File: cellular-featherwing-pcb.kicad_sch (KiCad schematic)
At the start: 42 parts, among them J1 SIM8060-6-0-14-00-A, J2 TSM-116-01-L-SV, J3 TSM-112-01-L-SV, J4 U.FL-R-SMT(10), J5 U.FL-R-SMT(10), U1 BG96, U2 TPS63020DSJR, U3 TXB0108DQSR, U4 MAX8868EUK30+

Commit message: schematic complete
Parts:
- added C1, C2, C6, C7, C8: 22uF, Capacitor_SMD:C_0603_1608Metric, symbol Device:C
- added C10, C13, C14, C9: DNP, Capacitor_SMD:C_0402_1005Metric, symbol Device:C
- added C12: 100pF, symbol Device:C
- added C15: 0.1uF, Capacitor_SMD:C_0402_1005Metric, symbol Device:C
- added C20, C21: 100nF, Capacitor_SMD:C_0402_1005Metric, symbol Device:C
- added C22, C3: 33pF, Capacitor_SMD:C_0402_1005Metric, symbol Device:C
- added C24, C25: 10pF, Capacitor_SMD:C_0402_1005Metric, symbol Device:C
- added C26, C28: C_Polarized_US, Capacitor_Tantalum_SMD:CP_EIA-3528-12_Kemet-T, symbol Device:C_Polarized_US
- added C3: 2.2uF, symbol Device:C
- added C30, C31, C33: 4.7uF, Capacitor_SMD:C_0402_1005Metric, symbol Device:C
- added C4: 0.1uF, symbol Device:C
- added FB1, FB2, FB3, FB4: FerriteBead, Resistor_SMD:R_0805_2012Metric, symbol Device:FerriteBead
- added L1: 1 uH, Inductor_SMD:L_Coilcraft_XxL4020, symbol pspice:INDUCTOR
- added L2: 47nH, symbol pspice:INDUCTOR
- added R1: 1.24M, symbol Device:R
- added R10, R16, R17: 10k, symbol Device:R
- added R11, R12, RR13: 1k, symbol Device:R
- added R15: 100k, symbol Device:R
- added R2: 182k, symbol Device:R
- added R6: 0, Capacitor_SMD:C_0402_1005Metric, symbol Device:R
- added R7: 10, Capacitor_SMD:C_0603_1608Metric, symbol Device:R
- added SC1, SC2: SolderJumper_2_Bridged, Jumper:SolderJumper-2_P1.3mm_Bridged_RoundedPad1.0x1.5mm, symbol Jumper:SolderJumper_2_Bridged
- added SO1, SO17, SO18, SO2: SolderJumper_2_Open, Jumper:SolderJumper-2_P1.3mm_Open_RoundedPad1.0x1.5mm, symbol Jumper:SolderJumper_2_Open
- added TP1, TP10, TP11, TP12, TP13, TP14, TP15, TP2, TP3, TP4, TP5, TP6, TP7, TP8, TP9: TestPoint, TestPoint:TestPoint_Pad_D1.0mm, symbol Connector:TestPoint
- added VD1, VD2: D_TVS, symbol Device:D_TVS
- added VD5, VD6: SS2030FL_R1_00001, Diode_SMD:D_SOD-123F, symbol Device:D
- J4, J5: value U.FL-R-SMT(10) -> U.FL-R-SMT; Digikey (none) -> https://www.digikey.com/en/products/detail/hirose-electric-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; MP U.FL-R-SMT_10_ -> (none); MPN (none) -> U.FL-R-SMT(10)
- SC3, SC4, SC6, SC7, SO10, SO11, SO12, SO13, SO14, SO15, SO4, SO5, SO6, SO7, SO8: now left out of the parts list
- U1: Digikey (none) -> https://www.digikey.com/en/products/detail/quectel/BG96MA-1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; MPN (none) -> BG96MA-128-SGN
- U2: value TPS63020DSJR -> TPS63020QDSJTQ1; footprint IC_TPS63020DSJR -> TPS63020DSJR:IC_TPS63020DSJR; Availability Good -> (none); DigiKey-Purchase-URL https://snapeda.com/shop?store=DigiKey&id=296571 -> (none); Digikey (none) -> https://www.digikey.com/en/products/detail/texas-instrument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; MF Texas Instruments -> (none); MP TPS63020DSJR -> (none); MPN (none) -> TPS63020QDSJTQ1; Mouser-Purchase-URL https://snapeda.com/shop?store=Mouser&id=296571 -> (none); Package VSON-14 Texas Instruments -> (none); Price None -> (none); Texas_Instruments-Purchase-URL https://snapeda.com/shop?store=Texas+Instruments&id=296571 -> (none)
- U4: value MAX8868EUK30+ -> MAX8868EUK30+T; Digikey (none) -> https://www.digikey.com/en/products/detail/analog-devices-i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; MPN (none) -> MAX8868EUK30+T
- renumbered R2 to R21, R1 to R22
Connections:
- net 3V3: now also U4.4 (OUT), C31.1
- net 5V: now also VD6.2 (A)
- net CTS: now also SC1.2 (B)
- net CTS_GPS_TXD: now also SC1.1 (A), SO1.2 (B)
- net DBG_RXD: now also TP15.1
- net DBG_TXD: now also TP14.1
- net ENABLE: now also U2.12 (EN)
- net GND: now also J4.2, J4.3, J5.2, J5.3, U2.15 (PGND), U2.2 (GND), C1.2, C10.2, C13.2, C14.2, C15.2, C2.2, C20.2, C21.2, C22.2, C24.2, C25.2, C26.2, C28.2, C3.2, C3.2, C30.2, C31.2, C33.2, C4.2, C6.2, C7.2, C8.2, C9.2, R10.1, R15.2, R2.2, TP13.1, VD1.1 (A1), VD2.1 (A1)
- net GPS_ANT: now also C12.2, C14.1
- net GPS_ANT_VDD: now also C15.1, R7.2
- net GPS_RXD: now also SO2.1 (A)
- net GPS_TXD: now also SO1.1 (A)
- net GSM_ANT: now also C13.1, R6.2
- net GSM_CTS: now also TP4.1
- net GSM_DCD: now also TP6.1
- net GSM_DTR: now also TP5.1
- net GSM_RI: now also R11.2, TP7.1
- net GSM_RTS: now also TP3.1
- net GSM_RXD: now also TP2.1
- net GSM_STATUS: now also TP8.1
- net GSM_TXD: now also R12.2, RR13.2, TP1.1
- net I2C_SDA: now also R16.1
- net RI: now also R11.1
- net RTS: now also SC2.2 (B)
- net RTS_GPS_RXD: now also SC2.1 (A), SO2.2 (B)
- net TXD: now also R10.2, R12.1, RR13.1
- net USB_BOOT: now also TP12.1
- net USB_DN_GSM: now also TP11.1
- net USB_DP_GSM: now also TP10.1
- net USB_VBUS_GSM: now also TP9.1
- net VBAT: now also VD5.2 (A)
- net VBAT_RF: now also C20.1, C21.1, C22.1, C24.1, C25.1, C26.1, C28.1, C3.1, FB3.1, FB4.1
- net VDD: now also SO17.2 (B), SO18.2 (B)
- net VMODEM: now reaches U4.1 (~{SHDN})
- net VMODEM: now also U4.3 (IN), C30.1, FB2.2, FB3.2, FB4.2
- net at U4.5 (BP): now also C33.1
- net at J5.1: now also C10.1, C12.1, L2.1, VD2.2 (A2)
- net at J4.1: now also C9.1, R6.1, VD1.2 (A2)
- net at U2.1 (VINA): now also C4.1
- net at U2.10 (VIN_10): now also U2.11 (VIN_11), U2.13 (PS/SYNC), C1.1, C2.1, C3.1, FB1.2, R15.1
- net at U2.3 (FB): now also R1.2, R2.1
- net at U2.4 (VOUT_4): now also U2.5 (VOUT_5), C6.1, C7.1, C8.1, FB2.1, R1.1
- net at U2.6 (L2_6): now also U2.7 (L2_7), L1.1
- net at U2.8 (L1_8): now also U2.9 (L1_9), L1.2
- new net: L2.2, R7.1
- new net: R16.2, SO17.1 (A)
- new net: R17.2, SO18.1 (A)
- new net I2C_SCl: R17.1
- new net VIN: FB1.1, VD5.1 (K), VD6.1 (K)
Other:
- company: (none) -> Ribbit Network
- title: (none) -> Cellular Featherwing PCB
- moved on the sheet: C11, C16, C17, C18, C28, C29, C32, D1, DD1, J1, J4, R14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

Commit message: All footprints assigned
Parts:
- C11, C12, C16, C17, C18, C29, C3, C32, C4, R14: footprint (none) -> Capacitor_SMD:C_0402_1005Metric
- C34: renamed from C28; footprint (none) -> Capacitor_SMD:C_0402_1005Metric
- J2: MPN (none) -> TSM-116-01-L-SV
- J3: MPN (none) -> TSM-112-01-L-SV
- L2: footprint (none) -> Inductor_SMD:L_0402_1005Metric
- R1, R10, R11, R12, R15, R16, R17, R2, R8: footprint (none) -> Resistor_SMD:R_0402_1005Metric
- R13: renamed from RR13; footprint (none) -> Resistor_SMD:R_0402_1005Metric
- R21, R22, R3: footprint (none) -> Resistor_SMD:R_0402_1005Metric; Digikey (none) -> https://www.digikey.com/en/products/detail/yageo/RC0402JR-0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; MPN (none) -> RC0402JR-070RP
- R6: footprint Capacitor_SMD:C_0402_1005Metric -> Resistor_SMD:R_0402_1005Metric
- SC7: footprint (none) -> Jumper:SolderJumper-2_P1.3mm_Bridged_RoundedPad1.0x1.5mm
- VD1, VD2: footprint (none) -> Diode_SMD:D_0402_1005Metric
- VD4: footprint (none) -> LED_SMD:LED_0603_1608Metric; Digikey (none) -> https://www.digikey.com/en/products/detail/w%C3%BCrth-elekt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; MPN (none) -> 150060BS75000
- renumbered C3 to C23

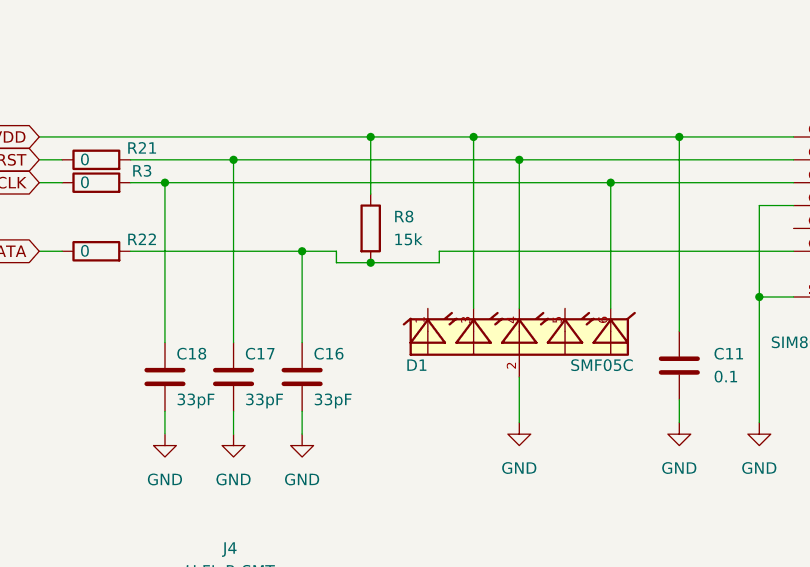
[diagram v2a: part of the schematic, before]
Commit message: Fixed drc and imported to pcb
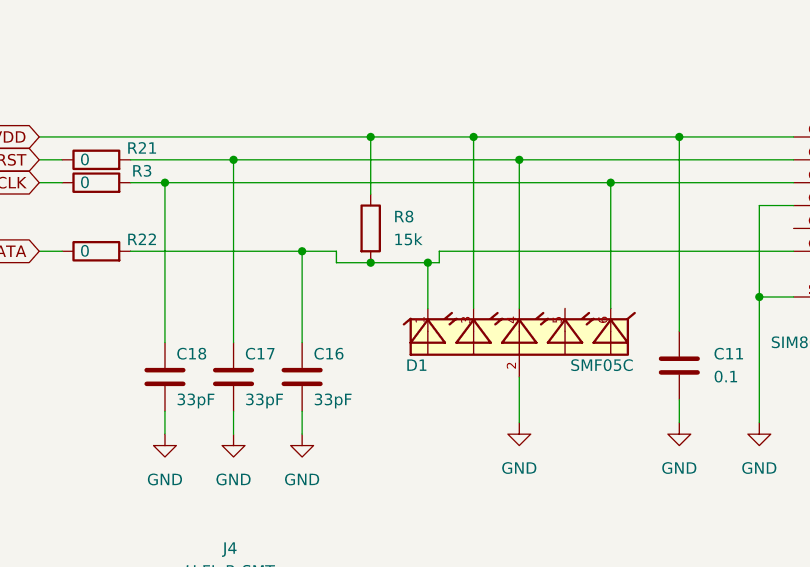
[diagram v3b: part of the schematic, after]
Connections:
- net at C16.1, J1.C7 (IO), R22.2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: now also D1.1
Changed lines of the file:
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@@
   (junction (at 379.73 45.72) (diameter 0) (color 0 0 0 0)
   )
+  (junction (at 71.12 114.3) (diameter 0) (color 0 0 0 0)
+  )
   (junction (at 64.77 100.33) (diameter 0) (color 0 0 0 0)
   )
@@
   (junction (at 107.95 118.11) (diameter 0) (color 0 0 0 0)
   )
+  (junction (at 118.11 41.91) (diameter 0) (color 0 0 0 0)
+  )
   (junction (at 224.79 215.9) (diameter 0) (color 0 0 0 0)
   )
@@
   (junction (at 92.71 195.58) (diameter 0) (color 0 0 0 0)
   )
-  (junction (at 118.11 41.91) (diameter 0) (color 0 0 0 0)
-  )
   (junction (at 91.44 105.41) (diameter 0) (color 0 0 0 0)
   )
@@
     (stroke (width 0) (type default) (color 0 0 0 0))
   )
+  (wire (pts (xy 114.3 41.91) (xy 118.11 41.91))
+    (stroke (width 0) (type default) (color 0 0 0 0))
+  )
   (wire (pts (xy 118.11 57.15) (xy 121.92 57.15))
     (stroke (width 0) (type default) (color 0 0 0 0))
@@
     (stroke (width 0) (type default) (color 0 0 0 0))
   )
-  (wire (pts (xy 64.77 114.3) (xy 72.39 114.3))
+  (wire (pts (xy 64.77 114.3) (xy 71.12 114.3))
     (stroke (width 0) (type default) (color 0 0 0 0))
   )
@@
     (stroke (width 0) (type default) (color 0 0 0 0))
   )
+  (wire (pts (xy 71.12 114.3) (xy 71.12 119.38))
+    (stroke (width 0) (type default) (color 0 0 0 0))
+  )
   (wire (pts (xy 377.19 58.42) (xy 382.27 58.42))
     (stroke (width 0) (type default) (color 0 0 0 0))
@@
     (stroke (width 0) (type default) (color 0 0 0 0))
   )
-  (wire (pts (xy 114.3 41.91) (xy 118.11 41.91))
-    (stroke (width 0) (type default) (color 0 0 0 0))
-  )
   (wire (pts (xy 59.69 152.4) (xy 72.39 152.4))
     (stroke (width 0) (type default) (color 0 0 0 0))
@@
     (stroke (width 0) (type default) (color 0 0 0 0))
   )
+  (wire (pts (xy 71.12 114.3) (xy 72.39 114.3))
+    (stroke (width 0) (type default) (color 0 0 0 0))
+  )

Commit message: Parts placement
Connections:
- net VBAT_BB: now also C21.1, C23.1, C25.1, C28.1, FB4.1
- net VBAT_RF: no longer C21.1, C23.1, C25.1, C28.1, FB4.1
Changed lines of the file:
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@@
     )
   )
-  (global_label "VBAT_RF" (shape bidirectional) (at 190.5 247.65 180) (fields_autoplaced)
+  (global_label "VBAT_BB" (shape bidirectional) (at 190.5 247.65 180) (fields_autoplaced)
     (effects (font (size 1.27 1.27)) (justify right))
-    (property "Intersheet References" "${INTERSHEET_REFS}" (id 0) (at 180.3459 247.5706 0)
+    (property "Intersheet References" "${INTERSHEET_REFS}" (id 0) (at 180.1645 247.5706 0)
       (effects (font (size 1.27 1.27)) (justify right) hide)
     )

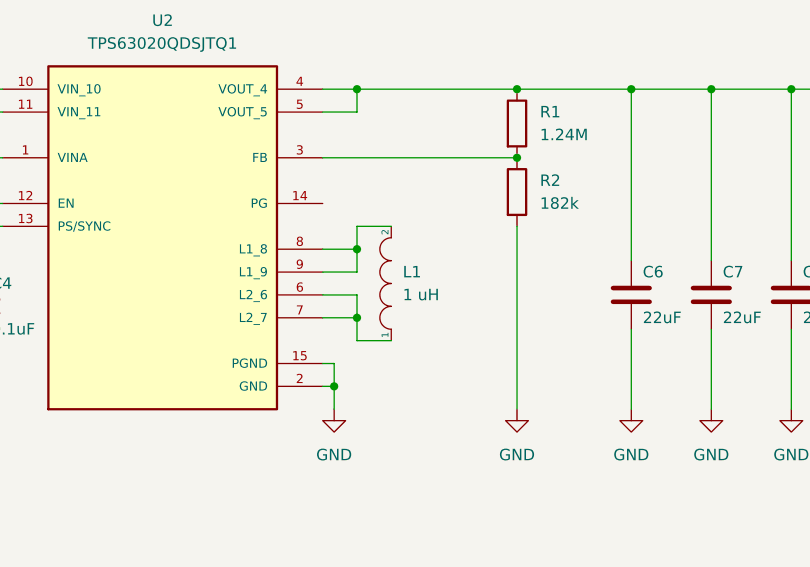
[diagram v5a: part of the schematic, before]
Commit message: Placed all components
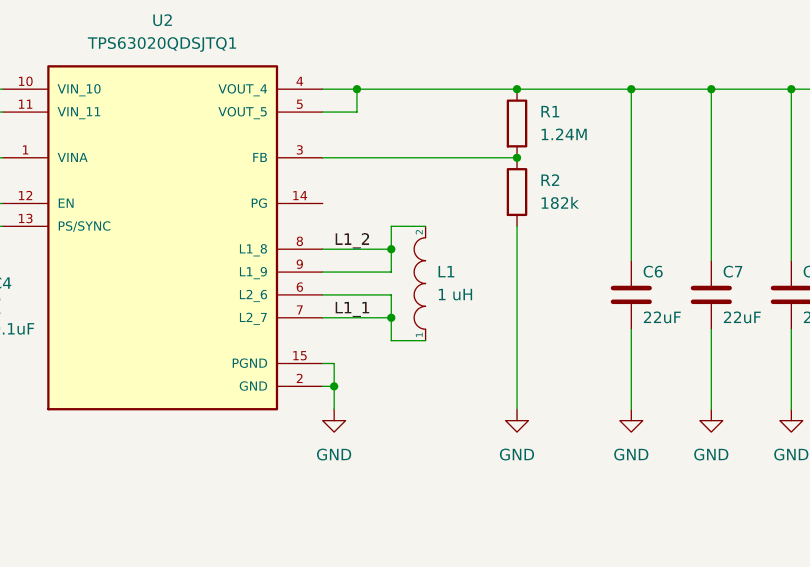
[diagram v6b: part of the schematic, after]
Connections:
- net L1_1: now reaches L1.1, U2.6 (L2_6), U2.7 (L2_7)
- net L1_2: now reaches L1.2, U2.8 (L1_8), U2.9 (L1_9)
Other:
- moved on the sheet: L1
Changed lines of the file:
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@@
   (junction (at 99.06 100.33) (diameter 0) (color 0 0 0 0)
   )
+  (junction (at 121.92 59.69) (diameter 0) (color 0 0 0 0)
+  )
   (junction (at 157.48 41.91) (diameter 0) (color 0 0 0 0)
   )
@@
   (junction (at 72.39 152.4) (diameter 0) (color 0 0 0 0)
   )
-  (junction (at 118.11 67.31) (diameter 0) (color 0 0 0 0)
+  (junction (at 121.92 67.31) (diameter 0) (color 0 0 0 0)
   )
   (junction (at 57.15 113.03) (diameter 0) (color 0 0 0 0)
@@
   (junction (at 115.57 74.93) (diameter 0) (color 0 0 0 0)
   )
-  (junction (at 118.11 59.69) (diameter 0) (color 0 0 0 0)
-  )
   (junction (at 72.39 195.58) (diameter 0) (color 0 0 0 0)
   )
@@
     (stroke (width 0) (type default) (color 0 0 0 0))
   )
-  (wire (pts (xy 118.11 67.31) (xy 118.11 69.85))
+  (wire (pts (xy 121.92 67.31) (xy 121.92 69.85))
     (stroke (width 0) (type default) (color 0 0 0 0))
   )
@@
     (stroke (width 0) (type default) (color 0 0 0 0))
   )
-  (wire (pts (xy 114.3 62.23) (xy 118.11 62.23))
+  (wire (pts (xy 114.3 62.23) (xy 121.92 62.23))
     (stroke (width 0) (type default) (color 0 0 0 0))
   )
@@
     (stroke (width 0) (type default) (color 0 0 0 0))
   )
-  (wire (pts (xy 118.11 57.15) (xy 121.92 57.15))
+  (wire (pts (xy 121.92 57.15) (xy 125.73 57.15))
     (stroke (width 0) (type default) (color 0 0 0 0))
   )
@@
     (stroke (width 0) (type default) (color 0 0 0 0))
   )
-  (wire (pts (xy 118.11 69.85) (xy 121.92 69.85))
+  (wire (pts (xy 121.92 69.85) (xy 125.73 69.85))
     (stroke (width 0) (type default) (color 0 0 0 0))
   )
@@
     (stroke (width 0) (type default) (color 0 0 0 0))
   )
-  (wire (pts (xy 118.11 64.77) (xy 118.11 67.31))
+  (wire (pts (xy 121.92 64.77) (xy 121.92 67.31))
     (stroke (width 0) (type default) (color 0 0 0 0))
   )
@@
     (stroke (width 0) (type default) (color 0 0 0 0))
   )
-  (wire (pts (xy 118.11 59.69) (xy 118.11 62.23))
+  (wire (pts (xy 121.92 59.69) (xy 121.92 62.23))
     (stroke (width 0) (type default) (color 0 0 0 0))
   )
@@
     (stroke (width 0) (type default) (color 0 0 0 0))
   )
-  (wire (pts (xy 114.3 64.77) (xy 118.11 64.77))
+  (wire (pts (xy 114.3 64.77) (xy 121.92 64.77))
     (stroke (width 0) (type default) (color 0 0 0 0))
   )
@@
     (stroke (width 0) (type default) (color 0 0 0 0))
   )
+  (wire (pts (xy 114.3 67.31) (xy 121.92 67.31))
+    (stroke (width 0) (type default) (color 0 0 0 0))
+  )
   (wire (pts (xy 38.1 102.87) (xy 49.53 102.87))
     (stroke (width 0) (type default) (color 0 0 0 0))
@@
     (stroke (width 0) (type default) (color 0 0 0 0))
   )
-  (wire (pts (xy 114.3 67.31) (xy 118.11 67.31))
-    (stroke (width 0) (type default) (color 0 0 0 0))
-  )
   (wire (pts (xy 327.66 179.07) (xy 332.74 179.07))
     (stroke (width 0) (type default) (color 0 0 0 0))
@@
     (stroke (width 0) (type default) (color 0 0 0 0))
   )
-  (wire (pts (xy 114.3 59.69) (xy 118.11 59.69))
+  (wire (pts (xy 114.3 59.69) (xy 121.92 59.69))
     (stroke (width 0) (type default) (color 0 0 0 0))
   )
@@
     (stroke (width 0) (type default) (color 0 0 0 0))
   )
-  (wire (pts (xy 118.11 59.69) (xy 118.11 57.15))
+  (wire (pts (xy 121.92 59.69) (xy 121.92 57.15))
     (stroke (width 0) (type default) (color 0 0 0 0))
   )
@@
     (stroke (width 0) (type default) (color 0 0 0 0))
   )
+  (label "L1_2" (at 115.57 59.69 0)
+    (effects (font (size 1.27 1.27)) (justify left bottom))
+  )
+  (label "L1_1" (at 115.57 67.31 0)
+    (effects (font (size 1.27 1.27)) (justify left bottom))
+  )
   (global_label "Q_INT" (shape bidirectional) (at 106.68 251.46 0) (fields_autoplaced)
     (effects (font (size 1.27 1.27)) (justify left))
@@
     (pin "1")
   )
-  (symbol (lib_id "pspice:INDUCTOR") (at 121.92 63.5 90) (unit 1)
+  (symbol (lib_id "pspice:INDUCTOR") (at 125.73 63.5 90) (unit 1)
     (in_bom yes) (on_board yes)
-    (property "Reference" "L1" (id 0) (at 123.19 62.2299 90)
+    (property "Reference" "L1" (id 0) (at 127 62.2299 90)
       (effects (font (size 1.27 1.27)) (justify right))
     )
-    (property "Value" "1 uH" (id 1) (at 123.19 64.7699 90)
+    (property "Value" "1 uH" (id 1) (at 127 64.7699 90)
       (effects (font (size 1.27 1.27)) (justify right))
     )
-    (property "Footprint" "Inductor_SMD:L_Coilcraft_XxL4020" (id 2) (at 121.92 63.5 0)
+    (property "Footprint" "Inductor_SMD:L_Coilcraft_XxL4020" (id 2) (at 125.73 63.5 0)
       (effects (font (size 1.27 1.27)) hide)
     )
-    (property "Datasheet" "~" (id 3) (at 121.92 63.5 0)
+    (property "Datasheet" "~" (id 3) (at 125.73 63.5 0)
       (effects (font (size 1.27 1.27)) hide)
     )
-    (property "MPN" "XGL4020-102MEC" (id 4) (at 125.73 55.88 90)
+    (property "MPN" "XGL4020-102MEC" (id 4) (at 129.54 55.88 90)
       (effects (font (size 1.27 1.27)) hide)
     )
-    (property "Digikey" "https://www.digikey.com/en/products/detail/coilcraft/XGL4020-102MEC/12714628?s=N4IgjCBcpgHAzFUBjKAzAhgGwM4FMAaEAeygG0R4B2ANgE4AWAJhCPlioFYAGCIhsGFo0QAXSIAHAC5QQAZSkAnAJYA7AOYgAvkTB1YdJCFSRMuQiXIhuYnSCbcORk2fxFSkCmAAEAVoASYpIykCAAqqrKUgDyaACyeBg4AK6KeNpEALQs0MZQSskWHhSctlkQuS7Ybpae9gycVGUgmQzO6NVFVghUvLZaWkA" (id 5) (at 121.92 63.5 90)
+    (property "Digikey" "https://www.digikey.com/en/products/detail/coilcraft/XGL4020-102MEC/12714628?s=N4IgjCBcpgHAzFUBjKAzAhgGwM4FMAaEAeygG0R4B2ANgE4AWAJhCPlioFYAGCIhsGFo0QAXSIAHAC5QQAZSkAnAJYA7AOYgAvkTB1YdJCFSRMuQiXIhuYnSCbcORk2fxFSkCmAAEAVoASYpIykCAAqqrKUgDyaACyeBg4AK6KeNpEALQs0MZQSskWHhSctlkQuS7Ybpae9gycVGUgmQzO6NVFVghUvLZaWkA" (id 5) (at 125.73 63.5 90)
       (effects (font (size 1.27 1.27)) hide)
     )

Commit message: All components placed
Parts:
- removed C10, C14: DNP, Capacitor_SMD:C_0402_1005Metric, symbol Device:C
- removed C12: 100pF, Capacitor_SMD:C_0402_1005Metric, symbol Device:C
- removed C15: 0.1uF, Capacitor_SMD:C_0402_1005Metric, symbol Device:C
- removed C32: 0.1, Capacitor_SMD:C_0402_1005Metric, symbol Device:C
- removed DD1: SN74AHC1G09DCKR, SN74AHC1G09DCKR:SN74AHC1G09DCKR, symbol 2023-01-14_23-42-37:SN74AHC1G09DCKR
- removed J5: U.FL-R-SMT, HRS_U.FL-R-SMT(10), symbol U.FL-R-SMT_10_:U.FL-R-SMT(10)
- removed L2: 47nH, Inductor_SMD:L_0402_1005Metric, symbol pspice:INDUCTOR
- removed R10, R16, R17: 10k, Resistor_SMD:R_0402_1005Metric, symbol Device:R
- removed R11, R12, R13: 1k, Resistor_SMD:R_0402_1005Metric, symbol Device:R
- removed R7: 10, Capacitor_SMD:C_0603_1608Metric, symbol Device:R
- removed SC1, SC2, SC3, SC4, SC6, SC7: SolderJumper_2_Bridged, Jumper:SolderJumper-2_P1.3mm_Bridged_RoundedPad1.0x1.5mm, symbol Jumper:SolderJumper_2_Bridged
- removed SO1, SO10, SO11, SO12, SO13, SO14, SO15, SO17, SO18, SO2, SO4, SO5, SO6, SO7, SO8, SO9: SolderJumper_2_Open, Jumper:SolderJumper-2_P1.3mm_Open_RoundedPad1.0x1.5mm, symbol Jumper:SolderJumper_2_Open
- removed TP7: TestPoint, TestPoint:TestPoint_Pad_D1.0mm, symbol Connector:TestPoint
- removed VD2: D_TVS, Diode_SMD:D_0402_1005Metric, symbol Device:D_TVS
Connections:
- net CTS_GPS_TXD is gone; now on net CTS: U3.4 (A4)
- net GSM_RXD_ESP32 is gone; now on net GSM_RXD: J2.15
- net GSM_TXD_ESP32 is gone; now on net GSM_TXD: J2.14
- net RTS_GPS_RXD is gone; now on net RTS: U3.3 (A3)
- net VDD: now also VD4.2 (A)
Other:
- moved on the sheet: C13, C9, J4, R6, TP1, TP10, TP11, TP12, TP13, TP14, TP15, TP2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
